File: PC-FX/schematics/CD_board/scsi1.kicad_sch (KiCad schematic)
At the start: 70 parts, among them IC1 D78C14GF, IC107 XLJ6265AF-10LL, IC109 D6378GF, IC301 L7805, IC302 1951A, IC403 NLA904SF3P, IC409 XLJ6265AF-10LL, IC410 M27C256B-12F1, Q104 2SC2412K

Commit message: Progress mainly on SCSI chips and connections to the MCU
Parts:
- removed C150, C151: ?, Capacitor_SMD:C_0603_1608Metric, symbol Device:C
- removed C155: C, Capacitor_SMD:C_0603_1608Metric, symbol Device:C
- removed C159: ~, Capacitor_SMD:CP_Elec_5x5.4, symbol Device:C_Polarized
- removed C300, C301: 470uF, Capacitor_SMD:CP_Elec_8x10.5, symbol Device:C_Polarized
- removed C302: 100uF, Capacitor_SMD:CP_Elec_5x5.4, symbol Device:C_Polarized
- removed CF102: Crystal, symbol Device:Crystal
- removed D301: D, symbol Device:D
- removed IC1: D78C14GF, CDR-30A:PQFP-64_20x14mm_P1.0mm, symbol PC-Engine_CDR-30:D78C14GF
- removed IC107: XLJ6265AF-10LL, Package_SO:SOIC-28W_7.5x17.9mm_P1.27mm, symbol PC-FX:XLJ6265AF-10LL
- removed IC301: L7805, Package_TO_SOT_THT:TO-220-3_Horizontal_TabDown, symbol Regulator_Linear:L7805
- removed IC302: 1951A, Package_TO_SOT_SMD:SOT-89-3, symbol PC-Engine_CDR-30:1951A
- removed JK103: Barrel_Jack_Switch, symbol Connector:Barrel_Jack_Switch
- removed JK104: 30P_ELCO_5061, symbol PC-Engine_CDR-30:30P_ELCO_5061
- removed Q104: 2SC2412K, Package_TO_SOT_SMD:SOT-23, symbol PC-Engine_CDR-30:2SC2412K
- removed R160: 560, Resistor_SMD:R_0603_1608Metric, symbol Device:R
- removed R165: 68k, Resistor_SMD:R_0603_1608Metric, symbol Device:R
- removed R166: 100k, Resistor_SMD:R_0603_1608Metric, symbol Device:R
- removed R167: 3k3, Resistor_SMD:R_0603_1608Metric, symbol Device:R
- removed R175, R176, R177, R178, R179, R180, R181, R182, R183, R184, R185, R186, R187, R188, R189, R190, R191, R192, R193, R194, R196, R197, R308: 4.7k, Resistor_SMD:R_0603_1608Metric, symbol Device:R
- removed R514, R516, R534: 0, Resistor_SMD:R_0603_1608Metric, symbol Device:R
- removed R515, R519, R520, R521, R522, R523, R524, R525, R526: 220, Resistor_SMD:R_0603_1608Metric, symbol Device:R
- removed R517, R518, R527: 100, Resistor_SMD:R_0603_1608Metric, symbol Device:R
- added C407: ~, Capacitor_SMD:CP_Elec_5x5.4, symbol Device:C_Polarized
- added IC2, IC411: TC514256AP, Package_SO:SOJ-36_10.16x23.49mm_P1.27mm, symbol PC-FX:TC514256AP
- added IC408: XLJ6265AF-10LL, Package_SO:SOIC-28W_7.5x17.9mm_P1.27mm, symbol PC-FX:XLJ6265AF-10LL
- added R1: 10k, Resistor_SMD:R_0603_1608Metric, symbol Device:R
- added R405: R_Network09, Resistor_THT:R_Array_SIP10, symbol Device:R_Network09
- added R410, R411: 220, symbol Device:R_Pack04
- added R449: 220, Resistor_SMD:R_0603_1608Metric, symbol Device:R
- added R482: 470k, Resistor_SMD:R_0603_1608Metric, symbol Device:R
- added R483, R484: 470, Resistor_SMD:R_0603_1608Metric, symbol Device:R
- added R485, R486: ~, Resistor_SMD:R_0603_1608Metric, symbol Device:R
- added X402: Crystal_GND2, symbol Device:Crystal_GND2
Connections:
- net I2S_DAT is gone; now on net DOUT: IC109.86 (DATA)
- net I2S_LRCK is gone; now on net LRCK: IC109.88 (LRCK)
- net MA13 is gone; now on net PF5: IC410.26 (A13)
- net MA14 is gone; now on net PF6: IC410.27 (A14)
- net ~{EEPROM_CE} is gone; now on net PF7: IC410.20 (~{E})
- net ~{I2S_SCLK} is gone; now on net BCLK: IC109.87 (BCLK)
- net ~{SCSI_ACK} is gone; now on net IC403_P74: IC109.33 (FS2)
- net ~{SCSI_IO} is gone; now on net IC403_P98: IC109.35 (FS1)
- net +5V: now also C407.1, IC408.26 (CE2), IC408.28 (VCC); no longer C152.2, IC109.100, IC109.2, IC109.29, IC109.31, IC109.34, IC109.36, IC109.37, IC109.48, IC109.52, IC109.79, IC109.85, IC109.91
- net ALE: now also IC403.31 (ALE)
- net GND: now also IC403.14 (GND), IC403.30 (GND), IC403.51 (GND), IC403.73 (GND), IC403.80 (GND), C407.2, IC2.26 (VSS), IC408.14 (VSS), IC411.26 (VSS), X402.2; no longer IC109.98
- net MA0: now also IC403.81 (MA0), IC408.10 (A0); no longer IC109.66 (MA0), IC409.10 (A0)
- net MA1: now also IC403.82 (MA1), IC408.9 (A1); no longer IC109.67 (MA1), IC409.9 (A1)
- net MA2: now also IC403.83 (MA2), IC408.8 (A2); no longer IC109.68 (MA2), IC409.8 (A2)
- net MA3: now also IC403.84 (MA3), IC408.7 (A3); no longer IC109.69 (MA3), IC409.7 (A3)
- net MA4: now also IC403.85 (MA4), IC408.6 (A4); no longer IC109.70 (MA4), IC409.6 (A4)
- net MA5: now also IC403.86 (MA5), IC408.5 (A5); no longer IC109.71 (MA5), IC409.5 (A5)
- net MA6: now also IC403.87 (MA6), IC408.4 (A6); no longer IC109.72 (MA6), IC409.4 (A6)
- net MA7: now also IC403.88 (MA7), IC408.3 (A7); no longer IC109.73 (MA7), IC409.3 (A7)
- net MD0: no longer IC410.11 (Q0)
- net MD1: no longer IC410.12 (Q1)
- net MD2: no longer IC410.13 (Q2)
- net MD3: no longer IC410.15 (Q3)
- net MD4: no longer IC410.16 (Q4)
- net MD5: no longer IC410.17 (Q5)
- net MD6: no longer IC410.18 (Q6)
- net MD7: no longer IC410.19 (Q7)
- net PD0: now also IC403.22 (PD0), IC410.11 (Q0), IC408.11 (D0)
- net PD1: now also IC403.21 (PD1), IC410.12 (Q1), IC408.12 (D1)
- net PD2: now also IC403.20 (PD2), IC410.13 (Q2), IC408.13 (D2)
- net PD3: now also IC403.19 (PD3), IC410.15 (Q3), IC408.15 (D3)
- net PD4: now also IC403.18 (PD4), IC410.16 (Q4), IC408.16 (D4)
- net PD5: now also IC403.17 (PD5), IC410.17 (Q5), IC408.17 (D5)
- net PD6: now also IC403.16 (PD6), IC410.18 (Q6), IC408.18 (D6)
- net PD7: now also IC403.15 (PD7), IC410.19 (Q7), IC408.19 (D7)
- net PF0: now also IC410.25 (A8), IC408.25 (A8)
- net PF1: now also IC410.24 (A9), IC408.24 (A9)
- net PF2: now also IC410.21 (A10), IC408.21 (A10)
- net PF3: now also IC410.23 (A11), IC408.23 (A11)
- net PF4: now also IC410.2 (A12), IC408.2 (A12)
- net PF5: now also IC403.26 (PF5); no longer IC109.12 (F5)
- net SCSI_D0: now also IC403.13 (SCSI_D0); no longer IC109.46 (FX0)
- net SCSI_D1: now also IC403.12 (SCSI_D1); no longer IC109.45 (FX1)
- net SCSI_D2: now also IC403.11 (SCSI_D2); no longer IC109.44 (FX2)
- net SCSI_D3: now also IC403.10 (SCSI_D3); no longer IC109.43 (FX3)
- net SCSI_D4: now also IC403.9 (SCSI_D4); no longer IC109.42 (FX4)
- net SCSI_D5: now also IC403.8 (SCSI_D5); no longer IC109.41 (FX5)
- net SCSI_D6: now also IC403.7 (SCSI_D6); no longer IC109.39 (FX6)
- net SCSI_D7: now also IC403.6 (SCSI_D7); no longer IC109.38 (FX7)
- net ~{MRST}: now also IC109.49 (~{RESET1}), IC403.70 (~{RESET})
- net ~{RD}: now also R478.1, IC408.22 (~{OE})
- net ~{WR}: now also IC403.32 (~{WE}), R477.1, IC408.27 (~{WE})
- net VCC: now reaches IC403.1 (VCC)
- net VCC: now also C152.2, IC109.100 (VCC), IC109.12 (F5), IC109.2 (VCC), IC109.29 (VCC), IC109.31 (VCC), IC109.34 (VCC), IC109.36 (VCC), IC109.37 (VCC), IC109.48 (VCC), IC109.52 (VCC), IC109.79 (VCC), IC109.85 (VCC), IC109.91 (VCC), IC403.39 (VCC), IC403.48 (VCC), IC403.64 (VCC), IC403.71 (VCC), IC403.72 (VCC), IC403.89 (VCC), IC403.95 (VCC), IC2.13 (VCC), IC411.13 (VCC), R1.2, R405.1 (common)
- net at IC403.100 (SRAM_~{CE}): now also IC408.20 (~{CE1})
- net IC403_P23: now reaches IC403.23
- net IC403_P23: now also IC109.25 (MA12)
- net PF7: now reaches IC403.24 (PF7)
- net PF6: now reaches IC403.25 (PF6)
- net at IC403.34 (?): now also IC403.35 (?)
- net at IC403.36 (?): now also IC403.37 (?)
- net at IC403.38: now also R1.1
- net DRAM_D0: now reaches IC403.40 (D0)
- net DRAM_D0: now also IC109.46 (FX0), IC411.1 (I/O1), R405.10 (R9)
- net DRAM_D1: now reaches IC403.41 (D1)
- net DRAM_D1: now also IC109.45 (FX1), IC411.2 (I/O2), R405.2 (R1)
- net DRAM_D2: now reaches IC403.42 (D2)
- net DRAM_D2: now also IC109.44 (FX2), IC411.24 (I/O3), R405.9 (R8)
- net DRAM_D3: now reaches IC403.43 (D3)
- net DRAM_D3: now also IC109.43 (FX3), IC411.25 (I/O4), R405.3 (R2)
- net DRAM_D4: now reaches IC403.44 (D4)
- net DRAM_D4: now also IC109.42 (FX4), IC2.1 (I/O1), R405.8 (R7)
- net DRAM_D5: now reaches IC403.45 (D5)
- net DRAM_D5: now also IC109.41 (FX5), IC2.2 (I/O2), R405.4 (R3)
- net DRAM_D6: now reaches IC403.46 (D6)
- net DRAM_D6: now also IC109.39 (FX6), IC2.24 (I/O3), R405.7 (R6)
- net DRAM_D7: now reaches IC403.47 (D7)
- net DRAM_D7: now also IC109.38 (FX7), IC2.25 (I/O4), R405.5 (R4)
- net at IC403.49 (XO): now also R482.2, X402.3
- net at IC403.50 (XI): now also R482.1, X402.1
- net at IC403.55 (A0): now also R411.8 (R1.2)
- net at IC403.56 (A1): now also R411.7 (R2.2)
- net at IC403.57 (A2): now also R411.6 (R3.2)
- net IC403_P74: now reaches IC403.74
- net DOUT: now reaches IC403.90 (DOUT)
- net BCLK: now reaches IC403.91 (BCLK)
- net WDCK: now reaches IC403.92 (WDCK)
- net SCOR: now reaches IC403.93 (SCOR)
- net LRCK: now reaches IC403.94 (LRCK)
- net CN401_P26: now reaches IC403.96 (?)
- net CN401_P18: now reaches IC403.97 (?)
- net IC403_P98: now reaches IC403.98
- net IC403_P99: now reaches IC403.99
- net IC403_P99: now also IC109.98
- net XTAO: now reaches IC109.90 (XIN)
- net at IC109.84 (~{CWE}), IC409.27 (~{WE}): no longer R478.1
- net IC402_P21: now reaches IC109.21
- net IC402_P22: now reaches IC109.22
- net IC402_P23: now reaches IC109.23
- net DOUBLE_SPEED: now reaches IC109.24
- net IC403_P69: now reaches IC109.26 (MA11)
- net IC403_P69: now also IC403.69
- net CN401_P27: now reaches IC109.27 (MA10)
- net CN401_P8: now reaches IC109.30 (MA9)
- net MA10: no longer names the net of IC109.76 (MA10), IC409.21 (A10)
- net MA10: no longer IC410.21 (A10)
- net MA11: no longer names the net of IC109.77 (MA11), IC409.23 (A11)
- net MA11: no longer IC410.23 (A11)
- net MA12: no longer names the net of IC109.78 (MA12), IC409.2 (A12)
- net MA12: no longer IC410.2 (A12)
- net MA8: no longer names the net of IC109.74 (MA8), IC409.25 (A8)
- net MA8: no longer IC410.25 (A8)
- net MA9: no longer names the net of IC109.75 (MA9), IC409.24 (A9)
- net MA9: no longer IC410.24 (A9)
- net PA0: no longer names the net of IC109.94 (PA0)
- net PA1 renamed IC402_P95
- net PA2 renamed IC402_P96
- net UPC3 renamed IC402_P93
- net ~{SCSI_ATN?} renamed CN401_P17
- net ~{SCSI_BSY} renamed CN401_P23
- net ~{SCSI_CD} renamed CN401_P19
- net ~{SCSI_MSG} renamed CN401_P20
- net ~{SCSI_REQ} renamed IC403_P75
- net IC403_P75: now also IC403.75
- new net: IC403.59 (A4), R449.2
- new net: IC403.58 (A3), R411.5 (R4.2)
- new net: IC403.60 (A5), R410.8 (R1.2)
- new net: IC403.61 (A6), R410.7 (R2.2)
- new net: IC403.62 (A7), R410.6 (R3.2)
- new net: IC403.63 (A8), R410.5 (R4.2)
- new net: IC403.65 (DRAM_~{RAS}), R483.1
- new net: IC403.66 (DRAM_~{CAS}), R484.2
- new net: IC109.66 (MA0), IC409.10 (A0)
- new net: IC109.73 (MA7), IC409.3 (A7)
- new net: IC109.72 (MA6), IC409.4 (A6)
- new net: IC109.71 (MA5), IC409.5 (A5)
- new net: IC109.70 (MA4), IC409.6 (A4)
- new net: IC109.69 (MA3), IC409.7 (A3)
- new net: IC109.68 (MA2), IC409.8 (A2)
- new net: IC109.67 (MA1), IC409.9 (A1)
- new net DRAM_A0: IC2.9 (A0), IC411.9 (A0), R411.1 (R1.1)
- new net DRAM_A1: IC2.10 (A1), IC411.10 (A1), R411.2 (R2.1)
- new net DRAM_A2: IC2.11 (A2), IC411.11 (A2), R411.3 (R3.1)
- new net DRAM_A3: IC2.12 (A3), IC411.12 (A3), R411.4 (R4.1)
- new net DRAM_A4: IC2.14 (A4), IC411.14 (A4), R449.1
- new net DRAM_A5: IC2.15 (A5), IC411.15 (A5), R410.1 (R1.1)
- new net DRAM_A6: IC2.16 (A6), IC411.16 (A6), R410.2 (R2.1)
- new net DRAM_A7: IC2.17 (A7), IC411.17 (A7), R410.3 (R3.1)
- new net DRAM_A8: IC2.18 (A8), IC411.18 (A8), R410.4 (R4.1)
- new net DRAM_~{CAS}: IC2.23 (~{CAS}), IC411.23 (~{CAS}), R484.1
- new net DRAM_~{OE}: IC2.22 (~{OE}), IC403.67 (DRAM_~{OE}), IC411.22 (~{OE}), R485.1, R485.2
- new net DRAM_~{RAS}: IC2.4 (~{RAS}), IC411.4 (~{RAS}), R483.2
- new net DRAM_~{WRITE}: IC2.3 (~{WRITE}), IC403.68 (DRAM_~{WR}), IC411.3 (~{WRITE}), R486.1, R486.2
- no-connect marks 9 -> 22
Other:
- note added: "SCSI Gate Array 1"
- note added: "SCSI Gate Array 2"
- note removed: "Alternative 9V power input"
- note removed: "CDR-30 (older revision used D9309GF instead but seemed to be the same)"
- note removed: "CN401 P17"
- note removed: "CN401 P19"
- note removed: "CN401 P20"
- note removed: "CN401 P23"
- note removed: "CN401 P27 SEL or RST?"
- note removed: "CN401 P8 SEL or RST?"
- note removed: "IC403 P24"
- note removed: "In the CDR-30 Rev all of the series resistos, R511-R527, are not there."
- note removed: "MRST"
- note removed: "No R534 on CDR-30 Rev"
- note removed: "SCSI ASIC"
- note removed: "TO CN103 P6"
- moved on the sheet: C152, C415, C418, IC409

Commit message: Update on DSP sheet mainly.
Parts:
- removed C152: ?, Capacitor_SMD:C_0603_1608Metric, symbol Device:C
- added C419, C428, C429, C431: ~, Capacitor_SMD:CP_Elec_5x5.4, symbol Device:C_Polarized
- added C420, C452, C453: ~, Capacitor_SMD:C_0603_1608Metric, symbol Device:C
- added C423, C430, C451: ?, Capacitor_SMD:C_0603_1608Metric, symbol Device:C
- renumbered C418 to C416, C147 to C417, C416 to C418, R1 to R487
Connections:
- net +5V: now also C419.1, C420.1, C423.1, C428.1, C429.1, C430.1, C431.1, C451.1, C452.1, C453.1
- net GND: now also C419.2, C420.2, C423.2, C428.2, C429.2, C430.2, C431.2, C451.2, C452.2, C453.2
- net IC403_P69 renamed ~{INRST_EN}
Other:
- note added: "SCSI_~{ACK} ?"
- note added: "SCSI_~{BSY} ?"
- note added: "SCSI_~{CD} ?"
- note added: "SCSI_~{IO} ?"
- note added: "SCSI_~{MSG} ?"
- note added: "SCSI_~{REQ} ?"
- moved on the sheet: R487

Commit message: Schematics pretty much done. Expect some mistakes but it captures enough information to help understanding its behaviour.
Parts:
- IC109: symbol PC-Engine_CDR-30:D6378GF -> PC-FX:D6378GF
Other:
- note added: "Memory Map from MCU 0000-7FFF = 32KB EEPROM (IC410) C000-DFFF = 8KB SRAM (IC408) The MCU is a ROM less chip so all ROM accesses are done externally. A0-7 and D0-7 are multiplexed depending on the state of ALE. A0-7 is presented on the PD bus while ALE = '1'. The 2 gate arrays work differently. 1 latches the PD bus and the PF bus while the other one only latches the PD bus (i.e. only the address b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"
- note removed: "IC403 P23"
- note removed: "IC403 P25"
- note removed: "IC403 P26"
- title: PC FX Pots Adfustment Schematics -> PC-FX CD Board Schematics
- moved on the sheet: C407, C408, C415, C416, C417, C418, C419, C420, C423, C428, C429, C430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

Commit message: Small update based on confirmation of SCSI control signals
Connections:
- net CN401_P17 renamed SCSI_~{IO}
- net CN401_P18 renamed SCSI_~{REQ}
- net CN401_P19 renamed SCSI_~{CD}
- net CN401_P20 renamed SCSI_~{MSG}
- net CN401_P23 renamed SCSI_~{BSY}
- net CN401_P26 renamed SCSI_~{ACK}
- net CN401_P27 renamed SCSI_~{ATN}
- net IC402_P23 renamed SWITCH_STROBE
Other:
- note added: "P21, P22 and P23 are PWM signals but only P23 is used to strobe the lid and the end switch. It has a small duty cycle so perhaps it relies on the internal capacitance of the analog input and acts as a top up mechanism to provide enough voltage to detect that the lid is closed."
- note added: "SRAM_CEN low when PF7-5 = "110""
- note removed: "SCSI_~{ACK} ?"
- note removed: "SCSI_~{BSY} ?"
- note removed: "SCSI_~{CD} ?"
- note removed: "SCSI_~{IO} ?"
- note removed: "SCSI_~{MSG} ?"
- note removed: "SCSI_~{REQ} ?"
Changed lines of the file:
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@@
 	(wire
 		(pts
-			(xy 347.98 207.01) (xy 359.41 207.01)
+			(xy 347.98 194.31) (xy 359.41 194.31)
 		)
 		(stroke
@@
 		)
 	)
+	(wire
+		(pts
+			(xy 266.7 215.9) (xy 287.02 215.9)
+		)
+		(stroke
+			(width 0)
+			(type default)
+		)
+	)
 	(bus
 		(pts
@@
 	(wire
 		(pts
-			(xy 347.98 199.39) (xy 359.41 199.39)
+			(xy 347.98 201.93) (xy 359.41 201.93)
 		)
 		(stroke
@@
 	(wire
 		(pts
-			(xy 347.98 196.85) (xy 359.41 196.85)
+			(xy 347.98 199.39) (xy 359.41 199.39)
 		)
 		(stroke
@@
 	(wire
 		(pts
-			(xy 347.98 194.31) (xy 359.41 194.31)
+			(xy 347.98 196.85) (xy 359.41 196.85)
 		)
 		(stroke
@@
 	(wire
 		(pts
-			(xy 347.98 204.47) (xy 359.41 204.47)
+			(xy 347.98 207.01) (xy 359.41 207.01)
 		)
 		(stroke
@@
 	(wire
 		(pts
-			(xy 266.7 215.9) (xy 287.02 215.9)
-		)
-		(stroke
-			(width 0)
-			(type default)
-		)
-	)
-	(wire
-		(pts
 			(xy 140.97 78.74) (xy 151.13 78.74)
 		)
@@
 	(wire
 		(pts
-			(xy 347.98 201.93) (xy 359.41 201.93)
+			(xy 347.98 204.47) (xy 359.41 204.47)
 		)
 		(stroke
@@
 		)
 	)
-	(text "SCSI_~{ACK} ?"
-		(exclude_from_sim no)
-		(at 378.206 207.264 0)
-		(effects
-			(font
-				(size 1.27 1.27)
-			)
-		)
-	)
 	(text "SCSI\nGate Array 2"
 		(exclude_from_sim no)
@@
 		)
 	)
-	(text "SCSI_~{IO} ?"
-		(exclude_from_sim no)
-		(at 377.952 192.024 0)
-		(effects
-			(font
-				(size 1.27 1.27)
-			)
-		)
-	)
 	(text "8KB RAM"
 		(exclude_from_sim no)
@@
 		)
 	)
-	(text "SCSI_~{CD} ?"
-		(exclude_from_sim no)
-		(at 377.952 189.484 0)
-		(effects
-			(font
-				(size 1.27 1.27)
-			)
-		)
-	)
 	(text "32KB EEPROM"
 		(exclude_from_sim no)
@@
 		)
 	)
-	(text "SCSI\nGate Array 1"
-		(exclude_from_sim no)
-		(at 317.754 164.084 0)
-		(effects
-			(font
-				(size 4 4)
-				(thickness 0.8)
-				(bold yes)
-			)
-		)
-	)
-	(text "SCSI_~{REQ} ?"
+	(text "SRAM_CEN low when PF7-5 = \"110\""
 		(exclude_from_sim no)
-		(at 378.206 204.724 0)
+		(at 160.782 141.986 0)
 		(effects
 			(font
@@
 		)
 	)
-	(text "SCSI_~{MSG} ?"
+	(text "SCSI\nGate Array 1"
 		(exclude_from_sim no)
-		(at 377.952 186.944 0)
+		(at 317.754 164.084 0)
 		(effects
 			(font
-				(size 1.27 1.27)
+				(size 4 4)
+				(thickness 0.8)
+				(bold yes)
 			)
 		)
 	)
-	(text "SCSI_~{BSY} ?"
+	(text "P21, P22 and P23 are PWM signals but only P23 is used\nto strobe the lid and the end switch. \nIt has a small duty cycle so perhaps it relies on the internal\ncapacitance of the analog input and acts as a top up mechanism\nto provide enough voltage to detect that the lid is closed. "
 		(exclude_from_sim no)
-		(at 377.952 184.404 0)
+		(at 341.884 234.95 0)
 		(effects
 			(font
 				(size 1.27 1.27)
 			)
+			(justify left)
 		)
 	)
@@
 	)
 	(label "IC403_P99"
-		(at 359.41 194.31 180)
+		(at 359.41 196.85 180)
 		(fields_autoplaced yes)
 		(effects
@@
 	)
 	(label "IC403_P98"
-		(at 359.41 196.85 180)
+		(at 359.41 199.39 180)
 		(fields_autoplaced yes)
 		(effects
@@
 	)
 	(label "IC403_P74"
-		(at 359.41 199.39 180)
+		(at 359.41 201.93 180)
 		(fields_autoplaced yes)
 		(effects
@@
 	)
 	(label "IC403_P75"
-		(at 359.41 201.93 180)
+		(at 359.41 204.47 180)
 		(fields_autoplaced yes)
 		(effects
@@
 	(hierarchical_label "CN401_P8"
 		(shape output)
-		(at 359.41 204.47 0)
+		(at 359.41 207.01 0)
 		(fields_autoplaced yes)
 		(effects
@@
 		)
 	)
-	(hierarchical_label "CN401_P26"
-		(shape output)
+	(hierarchical_label "SCSI_~{ACK}"
+		(shape input)
 		(at 46.99 199.39 180)
 		(fields_autoplaced yes)
@@
 		)
 	)
-	(hierarchical_label "CN401_P23"
+	(hierarchical_label "SCSI_~{BSY}"
 		(shape output)
 		(at 359.41 184.15 0)
@@
 		)
 	)
-	(hierarchical_label "CN401_P19"
+	(hierarchical_label "SCSI_~{CD}"
 		(shape output)
 		(at 359.41 189.23 0)
@@
 		)
 	)
-	(hierarchical_label "CN401_P18"
+	(hierarchical_label "SCSI_~{REQ}"
 		(shape output)
 		(at 46.99 201.93 180)
@@
 		)
 	)
-	(hierarchical_label "CN401_P17"
+	(hierarchical_label "SCSI_~{IO}"
 		(shape output)
 		(at 359.41 191.77 0)
@@
 		)
 	)
-	(hierarchical_label "IC402_P23"
+	(hierarchical_label "SWITCH_STROBE"
 		(shape output)
 		(at 359.41 217.17 0)
@@
 		)
 	)
-	(hierarchical_label "CN401_P27"
-		(shape output)
-		(at 359.41 207.01 0)
+	(hierarchical_label "SCSI_~{ATN}"
+		(shape input)
+		(at 359.41 194.31 0)
 		(fields_autoplaced yes)
 		(effects
@@
 		)
 	)
-	(hierarchical_label "CN401_P20"
+	(hierarchical_label "SCSI_~{MSG}"
 		(shape output)
 		(at 359.41 186.69 0)

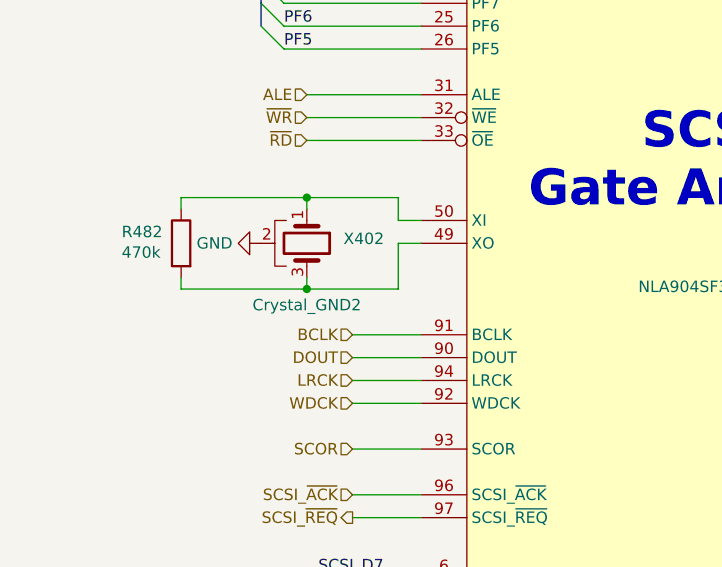
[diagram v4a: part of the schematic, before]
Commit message: Crystal frequency added + PDF of the schematics
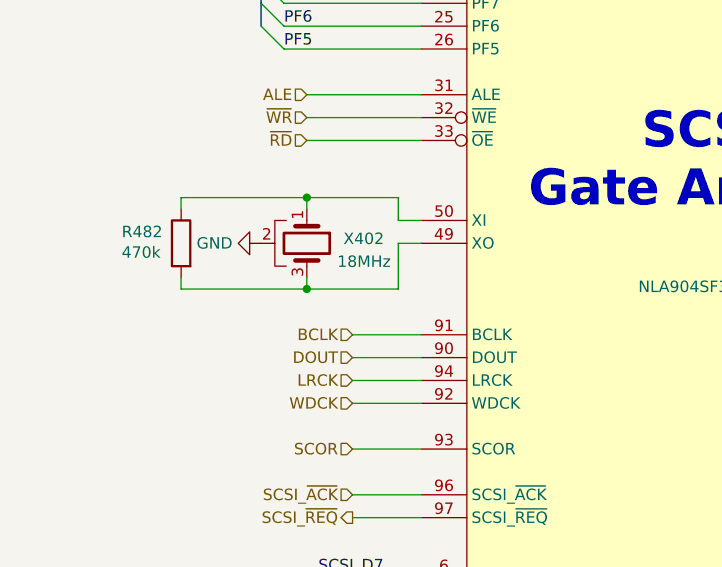
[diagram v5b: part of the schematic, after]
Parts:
- X402: value Crystal_GND2 -> 18MHz
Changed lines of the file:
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@@
 	(title_block
 		(title "PC-FX CD Board Schematics")
-		(date "2024-07-21")
+		(date "2024-07-25")
 		(rev "0.1")
 		(company "Author: Regis Galland")
@@
 			)
 		)
-		(property "Value" "Crystal_GND2"
-			(at 41.91 178.308 90)
+		(property "Value" "18MHz"
+			(at 48.26 173.482 90)
 			(effects
 				(font
